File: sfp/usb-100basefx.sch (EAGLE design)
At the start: 52 parts, among them IC1 LD33, IC2 93LC66SN, U1 AX88772BSP, U2 SFP, Y1 25MHz

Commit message: sfp: fixes
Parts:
- BOX1: value HAMMOND-BOX-H -> HAMMOND-BOX-H-1H; device hammond:HAMMOND-BOX-H -> hammond:HAMMOND-BOX-H-1H
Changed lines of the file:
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@@
 <grid distance="0.1" unitdist="inch" unit="inch" style="lines" multiple="1" display="no" altdistance="0.01" altunitdist="inch" altunit="inch"/>
 <layers>
-<layer number="1" name="Top" color="4" fill="1" visible="no" active="no"/>
-<layer number="16" name="Bottom" color="1" fill="1" visible="no" active="no"/>
-<layer number="17" name="Pads" color="2" fill="1" visible="no" active="no"/>
-<layer number="18" name="Vias" color="2" fill="1" visible="no" active="no"/>
-<layer number="19" name="Unrouted" color="6" fill="1" visible="no" active="no"/>
-<layer number="20" name="Dimension" color="15" fill="1" visible="no" active="no"/>
-<layer number="21" name="tPlace" color="7" fill="1" visible="no" active="no"/>
-<layer number="22" name="bPlace" color="7" fill="1" visible="no" active="no"/>
-<layer number="23" name="tOrigins" color="15" fill="1" visible="no" active="no"/>
-<layer number="24" name="bOrigins" color="15" fill="1" visible="no" active="no"/>
-<layer number="25" name="tNames" color="7" fill="1" visible="no" active="no"/>
-<layer number="26" name="bNames" color="7" fill="1" visible="no" active="no"/>
-<layer number="27" name="tValues" color="7" fill="1" visible="no" active="no"/>
-<layer number="28" name="bValues" color="7" fill="1" visible="no" active="no"/>
+<layer number="1" name="Top" color="4" fill="1" visible="yes" active="no"/>
+<layer number="16" name="Bottom" color="1" fill="1" visible="yes" active="no"/>
+<layer number="17" name="Pads" color="2" fill="1" visible="yes" active="no"/>
+<layer number="18" name="Vias" color="2" fill="1" visible="yes" active="no"/>
+<layer number="19" name="Unrouted" color="6" fill="1" visible="yes" active="no"/>
+<layer number="20" name="Dimension" color="15" fill="1" visible="yes" active="no"/>
+<layer number="21" name="tPlace" color="7" fill="1" visible="yes" active="no"/>
+<layer number="22" name="bPlace" color="7" fill="1" visible="yes" active="no"/>
+<layer number="23" name="tOrigins" color="15" fill="1" visible="yes" active="no"/>
+<layer number="24" name="bOrigins" color="15" fill="1" visible="yes" active="no"/>
+<layer number="25" name="tNames" color="7" fill="1" visible="yes" active="no"/>
+<layer number="26" name="bNames" color="7" fill="1" visible="yes" active="no"/>
+<layer number="27" name="tValues" color="7" fill="1" visible="yes" active="no"/>
+<layer number="28" name="bValues" color="7" fill="1" visible="yes" active="no"/>
 <layer number="29" name="tStop" color="7" fill="3" visible="no" active="no"/>
 <layer number="30" name="bStop" color="7" fill="6" visible="no" active="no"/>
@@
 <layer number="35" name="tGlue" color="7" fill="4" visible="no" active="no"/>
 <layer number="36" name="bGlue" color="7" fill="5" visible="no" active="no"/>
-<layer number="37" name="tTest" color="7" fill="1" visible="no" active="no"/>
-<layer number="38" name="bTest" color="7" fill="1" visible="no" active="no"/>
+<layer number="37" name="tTest" color="7" fill="1" visible="yes" active="no"/>
+<layer number="38" name="bTest" color="7" fill="1" visible="yes" active="no"/>
 <layer number="39" name="tKeepout" color="4" fill="11" visible="no" active="no"/>
 <layer number="40" name="bKeepout" color="1" fill="11" visible="no" active="no"/>
@@
 <layer number="44" name="Drills" color="7" fill="1" visible="no" active="no"/>
 <layer number="45" name="Holes" color="7" fill="1" visible="no" active="no"/>
-<layer number="46" name="Milling" color="3" fill="1" visible="no" active="no"/>
-<layer number="47" name="Measures" color="7" fill="1" visible="no" active="no"/>
-<layer number="48" name="Document" color="7" fill="1" visible="no" active="no"/>
-<layer number="49" name="Reference" color="7" fill="1" visible="no" active="no"/>
-<layer number="50" name="dxf" color="7" fill="1" visible="no" active="no"/>
-<layer number="51" name="tDocu" color="7" fill="1" visible="no" active="no"/>
-<layer number="52" name="bDocu" color="7" fill="1" visible="no" active="no"/>
-<layer number="53" name="tGND_GNDA" color="7" fill="9" visible="no" active="no"/>
-<layer number="54" name="bGND_GNDA" color="1" fill="9" visible="no" active="no"/>
-<layer number="56" name="wert" color="7" fill="1" visible="no" active="no"/>
+<layer number="46" name="Milling" color="3" fill="1" visible="yes" active="no"/>
+<layer number="47" name="Measures" color="7" fill="1" visible="yes" active="no"/>
+<layer number="48" name="Document" color="7" fill="1" visible="yes" active="no"/>
+<layer number="49" name="Reference" color="7" fill="1" visible="yes" active="no"/>
+<layer number="50" name="dxf" color="7" fill="1" visible="yes" active="no"/>
+<layer number="51" name="tDocu" color="7" fill="1" visible="yes" active="no"/>
+<layer number="52" name="bDocu" color="7" fill="1" visible="yes" active="no"/>
+<layer number="53" name="tGND_GNDA" color="7" fill="9" visible="yes" active="no"/>
+<layer number="54" name="bGND_GNDA" color="1" fill="9" visible="yes" active="no"/>
+<layer number="56" name="wert" color="7" fill="1" visible="yes" active="no"/>
 <layer number="91" name="Nets" color="2" fill="1" visible="yes" active="yes"/>
 <layer number="92" name="Busses" color="1" fill="1" visible="yes" active="yes"/>
@@
 <part name="U$1" library="SparkFun-Connectors" deviceset="USB-MINIB" device="-5PIN"/>
 <part name="U1" library="balto" deviceset="AX88772B" device="SP"/>
-<part name="BOX1" library="hammond" deviceset="HAMMOND-BOX" device="-H" value="HAMMOND-BOX-H"/>
+<part name="BOX1" library="hammond" deviceset="HAMMOND-BOX" device="-H-1H" value="HAMMOND-BOX-H-1H"/>
 <part name="C2" library="rcl" deviceset="C-EU" device="C0603" value="1u"/>
 <part name="P+3" library="supply1" deviceset="VCC" device=""/>

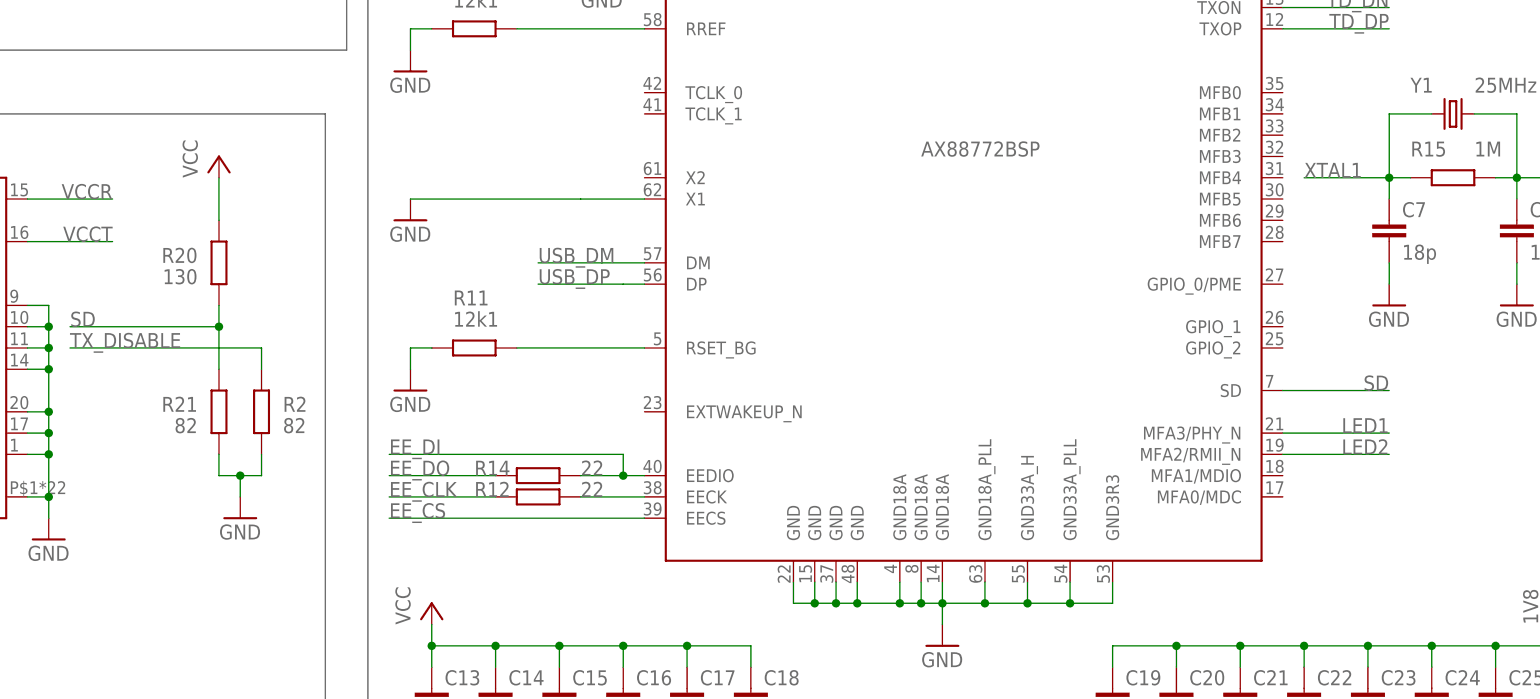
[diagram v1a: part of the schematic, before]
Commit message: rev1: fix sd signal logic level
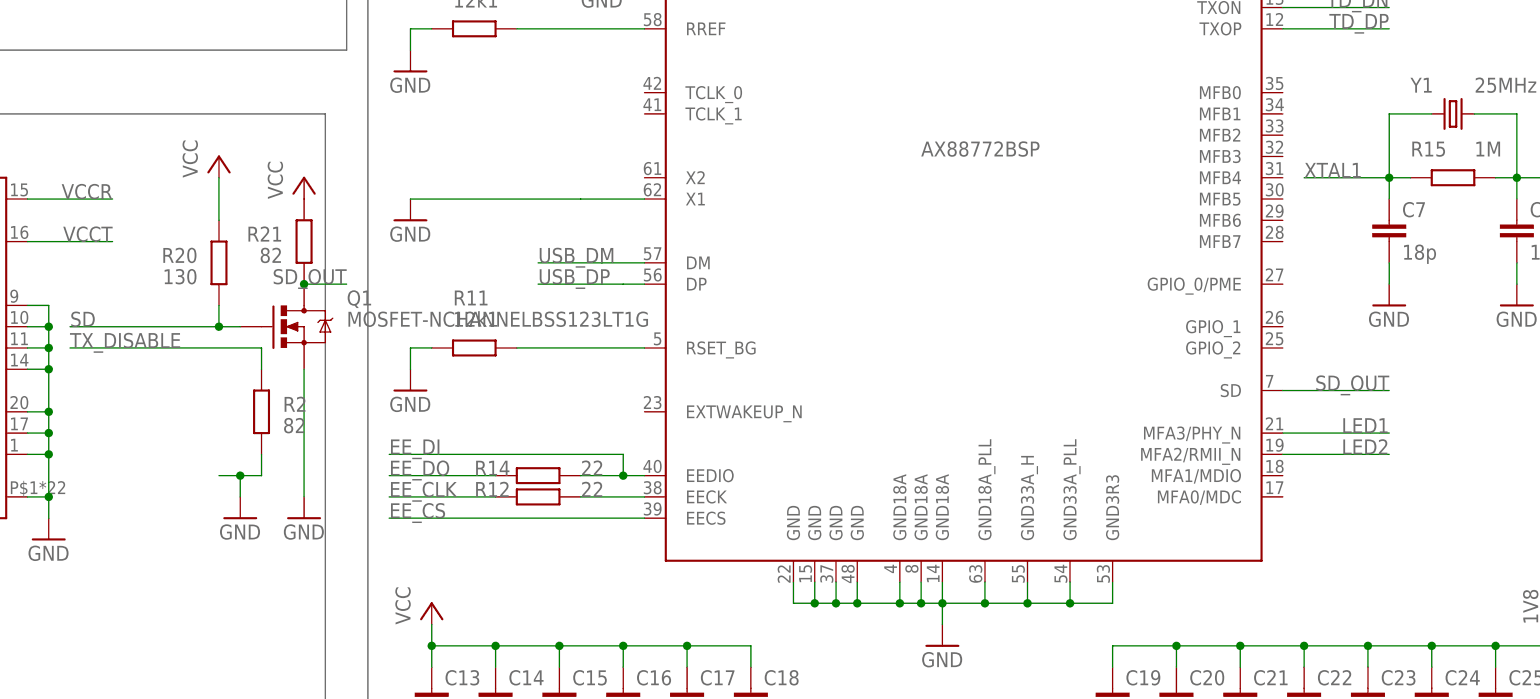
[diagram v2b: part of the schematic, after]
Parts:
- added Q1: MOSFET-NCHANNELBSS123LT1G, SparkFun-DiscreteSemi:MOSFET-NCHANNELBSS123LT1G
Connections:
- new net SD_OUT: Q1.D, R21.2, U1.SD
- net GND: now also Q1.S; no longer R21.2
- net SD: now also Q1.G; no longer R21.1, U1.SD
- net VCC: now also R21.1
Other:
- moved on the sheet: R21
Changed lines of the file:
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@@
 <grid distance="0.1" unitdist="inch" unit="inch" style="lines" multiple="1" display="no" altdistance="0.01" altunitdist="inch" altunit="inch"/>
 <layers>
-<layer number="1" name="Top" color="4" fill="1" visible="yes" active="no"/>
-<layer number="16" name="Bottom" color="1" fill="1" visible="yes" active="no"/>
-<layer number="17" name="Pads" color="2" fill="1" visible="yes" active="no"/>
-<layer number="18" name="Vias" color="2" fill="1" visible="yes" active="no"/>
-<layer number="19" name="Unrouted" color="6" fill="1" visible="yes" active="no"/>
-<layer number="20" name="Dimension" color="15" fill="1" visible="yes" active="no"/>
-<layer number="21" name="tPlace" color="7" fill="1" visible="yes" active="no"/>
-<layer number="22" name="bPlace" color="7" fill="1" visible="yes" active="no"/>
-<layer number="23" name="tOrigins" color="15" fill="1" visible="yes" active="no"/>
-<layer number="24" name="bOrigins" color="15" fill="1" visible="yes" active="no"/>
-<layer number="25" name="tNames" color="7" fill="1" visible="yes" active="no"/>
-<layer number="26" name="bNames" color="7" fill="1" visible="yes" active="no"/>
-<layer number="27" name="tValues" color="7" fill="1" visible="yes" active="no"/>
-<layer number="28" name="bValues" color="7" fill="1" visible="yes" active="no"/>
+<layer number="1" name="Top" color="4" fill="1" visible="no" active="no"/>
+<layer number="16" name="Bottom" color="1" fill="1" visible="no" active="no"/>
+<layer number="17" name="Pads" color="2" fill="1" visible="no" active="no"/>
+<layer number="18" name="Vias" color="2" fill="1" visible="no" active="no"/>
+<layer number="19" name="Unrouted" color="6" fill="1" visible="no" active="no"/>
+<layer number="20" name="Dimension" color="15" fill="1" visible="no" active="no"/>
+<layer number="21" name="tPlace" color="7" fill="1" visible="no" active="no"/>
+<layer number="22" name="bPlace" color="7" fill="1" visible="no" active="no"/>
+<layer number="23" name="tOrigins" color="15" fill="1" visible="no" active="no"/>
+<layer number="24" name="bOrigins" color="15" fill="1" visible="no" active="no"/>
+<layer number="25" name="tNames" color="7" fill="1" visible="no" active="no"/>
+<layer number="26" name="bNames" color="7" fill="1" visible="no" active="no"/>
+<layer number="27" name="tValues" color="7" fill="1" visible="no" active="no"/>
+<layer number="28" name="bValues" color="7" fill="1" visible="no" active="no"/>
 <layer number="29" name="tStop" color="7" fill="3" visible="no" active="no"/>
 <layer number="30" name="bStop" color="7" fill="6" visible="no" active="no"/>
@@
 <layer number="35" name="tGlue" color="7" fill="4" visible="no" active="no"/>
 <layer number="36" name="bGlue" color="7" fill="5" visible="no" active="no"/>
-<layer number="37" name="tTest" color="7" fill="1" visible="yes" active="no"/>
-<layer number="38" name="bTest" color="7" fill="1" visible="yes" active="no"/>
+<layer number="37" name="tTest" color="7" fill="1" visible="no" active="no"/>
+<layer number="38" name="bTest" color="7" fill="1" visible="no" active="no"/>
 <layer number="39" name="tKeepout" color="4" fill="11" visible="no" active="no"/>
 <layer number="40" name="bKeepout" color="1" fill="11" visible="no" active="no"/>
@@
 <layer number="44" name="Drills" color="7" fill="1" visible="no" active="no"/>
 <layer number="45" name="Holes" color="7" fill="1" visible="no" active="no"/>
-<layer number="46" name="Milling" color="3" fill="1" visible="yes" active="no"/>
-<layer number="47" name="Measures" color="7" fill="1" visible="yes" active="no"/>
-<layer number="48" name="Document" color="7" fill="1" visible="yes" active="no"/>
-<layer number="49" name="Reference" color="7" fill="1" visible="yes" active="no"/>
-<layer number="50" name="dxf" color="7" fill="1" visible="yes" active="no"/>
-<layer number="51" name="tDocu" color="7" fill="1" visible="yes" active="no"/>
-<layer number="52" name="bDocu" color="7" fill="1" visible="yes" active="no"/>
-<layer number="53" name="tGND_GNDA" color="7" fill="9" visible="yes" active="no"/>
-<layer number="54" name="bGND_GNDA" color="1" fill="9" visible="yes" active="no"/>
-<layer number="56" name="wert" color="7" fill="1" visible="yes" active="no"/>
+<layer number="46" name="Milling" color="3" fill="1" visible="no" active="no"/>
+<layer number="47" name="Measures" color="7" fill="1" visible="no" active="no"/>
+<layer number="48" name="Document" color="7" fill="1" visible="no" active="no"/>
+<layer number="49" name="Reference" color="7" fill="1" visible="no" active="no"/>
+<layer number="50" name="dxf" color="7" fill="1" visible="no" active="no"/>
+<layer number="51" name="tDocu" color="7" fill="1" visible="no" active="no"/>
+<layer number="52" name="bDocu" color="7" fill="1" visible="no" active="no"/>
+<layer number="53" name="tGND_GNDA" color="7" fill="9" visible="no" active="no"/>
+<layer number="54" name="bGND_GNDA" color="1" fill="9" visible="no" active="no"/>
+<layer number="56" name="wert" color="7" fill="1" visible="no" active="no"/>
 <layer number="91" name="Nets" color="2" fill="1" visible="yes" active="yes"/>
 <layer number="92" name="Busses" color="1" fill="1" visible="yes" active="yes"/>
@@
 <part name="GND22" library="supply1" deviceset="GND" device=""/>
 <part name="P+2" library="supply1" deviceset="VCC" device=""/>
+<part name="Q1" library="SparkFun-DiscreteSemi" deviceset="MOSFET-NCHANNEL" device="BSS123LT1G"/>
+<part name="GND23" library="supply1" deviceset="GND" device=""/>
+<part name="P+13" library="supply1" deviceset="VCC" device=""/>
 </parts>
 <sheets>
@@
 <attribute name="VALUE" x="91.44" y="104.14" size="1.778" layer="96" rot="MR0"/>
 </instance>
-<instance part="R21" gate="G$1" x="93.98" y="88.9" smashed="yes" rot="MR270">
-<attribute name="NAME" x="91.44" y="88.9" size="1.778" layer="95" rot="MR0"/>
-<attribute name="VALUE" x="91.44" y="86.36" size="1.778" layer="96" rot="MR0"/>
+<instance part="R21" gate="G$1" x="104.14" y="109.22" smashed="yes" rot="MR270">
+<attribute name="NAME" x="101.6" y="109.22" size="1.778" layer="95" rot="MR0"/>
+<attribute name="VALUE" x="101.6" y="106.68" size="1.778" layer="96" rot="MR0"/>
 </instance>
 <instance part="IC1" gate="G$1" x="119.38" y="27.94"/>
@@
 <instance part="GND22" gate="1" x="22.86" y="53.34"/>
 <instance part="P+2" gate="VCC" x="22.86" y="76.2"/>
+<instance part="Q1" gate="G$1" x="104.14" y="99.06"/>
+<instance part="GND23" gate="1" x="104.14" y="76.2"/>
+<instance part="P+13" gate="VCC" x="104.14" y="116.84"/>
 </instances>
 <busses>
@@
 <junction x="22.86" y="71.12"/>
 </segment>
+<segment>
+<pinref part="R21" gate="G$1" pin="1"/>
+<pinref part="P+13" gate="VCC" pin="VCC"/>
+</segment>
 </net>
 <net name="GND" class="0">
 <segment>
 <pinref part="GND3" gate="1" pin="GND"/>
-<pinref part="R21" gate="G$1" pin="2"/>
 <wire x1="96.52" y1="78.74" x2="96.52" y2="81.28" width="0.1524" layer="91"/>
 <wire x1="96.52" y1="81.28" x2="93.98" y2="81.28" width="0.1524" layer="91"/>
-<wire x1="93.98" y1="81.28" x2="93.98" y2="83.82" width="0.1524" layer="91"/>
 <pinref part="R2" gate="G$1" pin="2"/>
 <wire x1="96.52" y1="81.28" x2="99.06" y2="81.28" width="0.1524" layer="91"/>
@@
 <wire x1="22.86" y1="55.88" x2="22.86" y2="58.42" width="0.1524" layer="91"/>
 </segment>
+<segment>
+<pinref part="Q1" gate="G$1" pin="S"/>
+<pinref part="GND23" gate="1" pin="GND"/>
+<wire x1="104.14" y1="93.98" x2="104.14" y2="78.74" width="0.1524" layer="91"/>
+</segment>
 </net>
 <net name="TD_DP" class="0">
@@
 <segment>
 <label x="76.2" y="99.06" size="1.778" layer="95"/>
-<pinref part="R21" gate="G$1" pin="1"/>
-<wire x1="93.98" y1="93.98" x2="93.98" y2="99.06" width="0.1524" layer="91"/>
 <pinref part="R20" gate="G$1" pin="2"/>
 <wire x1="93.98" y1="99.06" x2="93.98" y2="101.6" width="0.1524" layer="91"/>
+<wire x1="93.98" y1="99.06" x2="76.2" y2="99.06" width="0.1524" layer="91"/>
+<pinref part="Q1" gate="G$1" pin="G"/>
+<wire x1="93.98" y1="99.06" x2="96.52" y2="99.06" width="0.1524" layer="91"/>
 <junction x="93.98" y="99.06"/>
-<wire x1="93.98" y1="99.06" x2="76.2" y2="99.06" width="0.1524" layer="91"/>
-</segment>
-<segment>
-<pinref part="U1" gate="G$1" pin="SD"/>
-<wire x1="220.98" y1="91.44" x2="233.68" y2="91.44" width="0.1524" layer="91"/>
-<label x="233.68" y="91.44" size="1.778" layer="95" rot="MR0"/>
 </segment>
 <segment>
@@
 </segment>
 </net>
+<net name="SD_OUT" class="0">
+<segment>
+<pinref part="Q1" gate="G$1" pin="D"/>
+<pinref part="R21" gate="G$1" pin="2"/>
+<wire x1="104.14" y1="104.14" x2="109.22" y2="104.14" width="0.1524" layer="91"/>
+<junction x="104.14" y="104.14"/>
+<label x="109.22" y="104.14" size="1.778" layer="95" rot="MR0"/>
+</segment>
+<segment>
+<pinref part="U1" gate="G$1" pin="SD"/>
+<wire x1="220.98" y1="91.44" x2="233.68" y2="91.44" width="0.1524" layer="91"/>
+<label x="233.68" y="91.44" size="1.778" layer="95" rot="MR0"/>
+</segment>
+</net>
